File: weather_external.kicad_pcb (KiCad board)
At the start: 2 copper layers, 28.2 x 51.6 mm, 31 parts, among them J1 Conn_01x02_Male, J2 USB_B_Mini, J3 Conn_01x02_Male, J4 Conn_01x02_Male, J8 FTDI, Q1 DMG2305UX-13, SW1 SW_Push, U1 MCP73831-2-OT, U2 MCP1700T-3302E_TT

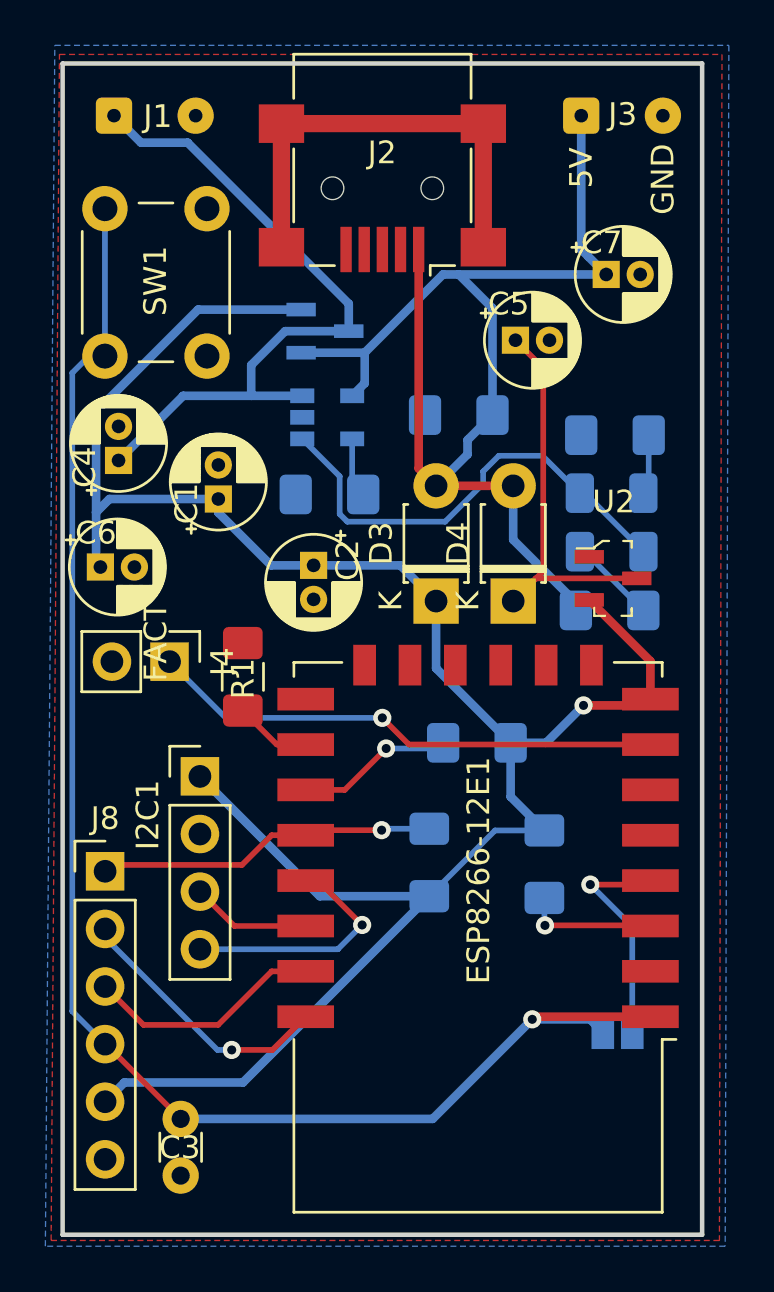
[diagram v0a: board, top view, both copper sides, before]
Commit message: V1.5 removing battery charger components
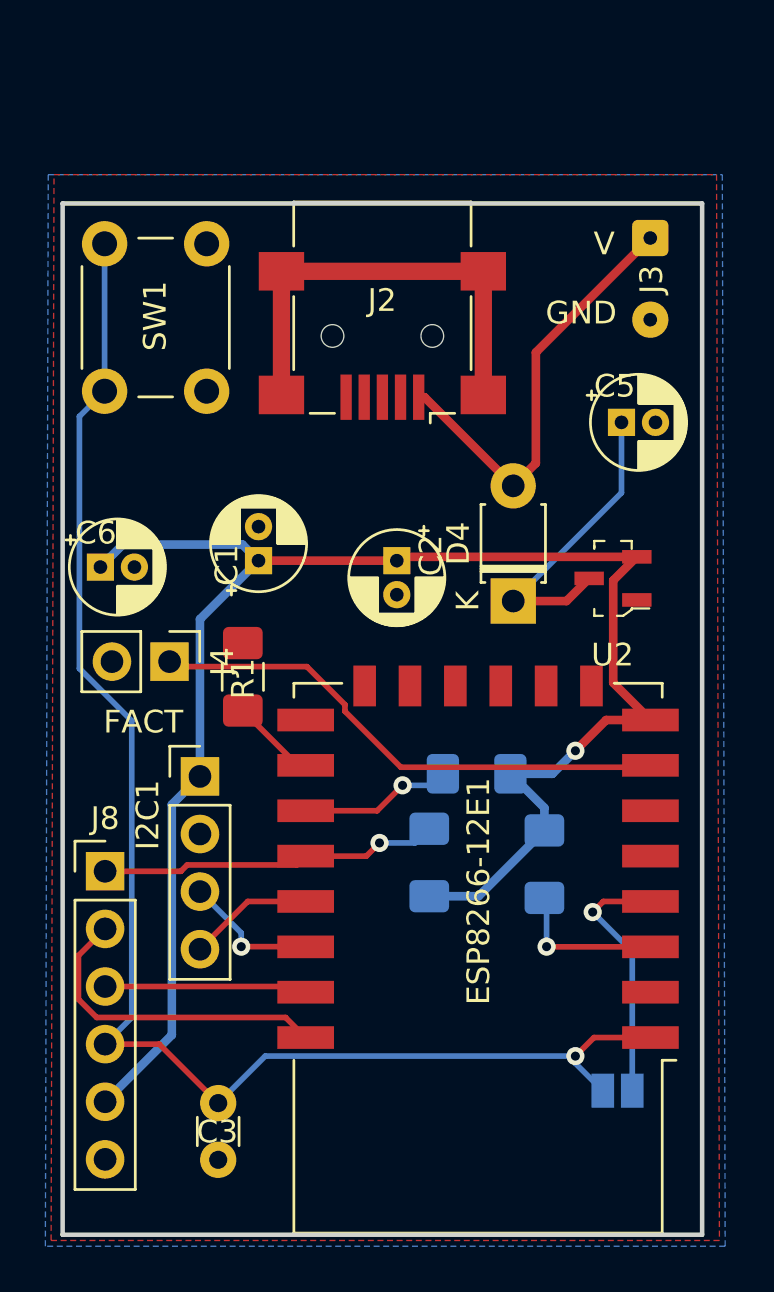
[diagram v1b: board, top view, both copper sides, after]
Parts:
- removed C4, C7: CP, Capacitor_THT:CP_Radial_D4.0mm_P1.50mm
- removed D1: GREEN, LED_SMD:LED_1206_3216Metric
- removed D2: RED, LED_SMD:LED_1206_3216Metric
- removed D3: 1N4148, Diode_THT:D_T-1_P5.08mm_Horizontal
- removed J1: Conn_01x02_Male, Connector_Wire:SolderWire-0.1sqmm_1x02_P3.6mm_D0.4mm_OD1mm
- removed Q1: DMG2305UX-13, digikey-footprints:SOT-23-3
- removed R5, R6: 220, Resistor_SMD:R_1206_3216Metric_Pad1.42x1.75mm_HandSolder
- removed R7: 2k, Resistor_SMD:R_1206_3216Metric_Pad1.42x1.75mm_HandSolder
- removed R8: 100k, Resistor_SMD:R_1206_3216Metric_Pad1.42x1.75mm_HandSolder
- removed U1: MCP73831-2-OT, Package_TO_SOT_SMD:SOT-23-5
- moved J2 6.51 mm to (10.0, 57.9)
- moved J3 6.19 mm to (21.8, 53.6), turned to 270 degrees
- moved C5 5.91 mm to (20.6, 61.7)
- moved C2 3.67 mm to (10.7, 67.8)
- moved C1 3.24 mm to (4.57, 67.8)
- moved JP1 2.59 mm to (20.4, 91.2)
- moved C3 1.79 mm to (2.79, 94.2)
- moved SW1 1.55 mm to (2.29, 53.8)
- moved R4 1.37 mm to (14.2, 77.2)
- moved ESP8266-12E1 0.92 mm to (14.2, 85.3)
- turned U2 to 180 degrees
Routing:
- net VCC: track 56.2 -> 19.2 mm
- net VBAT: track 30.5 -> 0.00 mm
- net Net-(D1-Pad2): track 20.8 -> 0.00 mm
- net +3V3: track 96.7 -> 75.9 mm
- net SDA: track 10.9 -> 5.53 mm, vias 1 -> 0
- net Net-(C5-Pad1): track 18.4 -> 13.6 mm
- net Net-(D2-Pad2): track 3.87 -> 0.00 mm
- net RST: track 69.3 -> 65.6 mm
- net Net-(D1-Pad1): track 2.65 -> 0.00 mm
- net Net-(R7-Pad2): track 2.65 -> 0.00 mm
- net TX: track 12.4 -> 14.3 mm, vias 1 -> 0
- net RX: track 10.5 -> 8.95 mm
- net GPIO16: track 9.99 -> 11.3 mm
- net EN: track 5.88 -> 6.77 mm
- net SCL: track 5.29 -> 6.02 mm, vias 0 -> 1
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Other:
- board size 28.2 x 51.6 mm -> 28.2 x 45.5 mm
- board text added: "Weather External v1.5"
- board text removed: "3V3"
- board text removed: "5V"
- board text removed: "SOLAR PANEL"
- board text removed: "Weather External v1.4"

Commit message: V 1.5 - no load management once it is built to run in solar panel charging mode
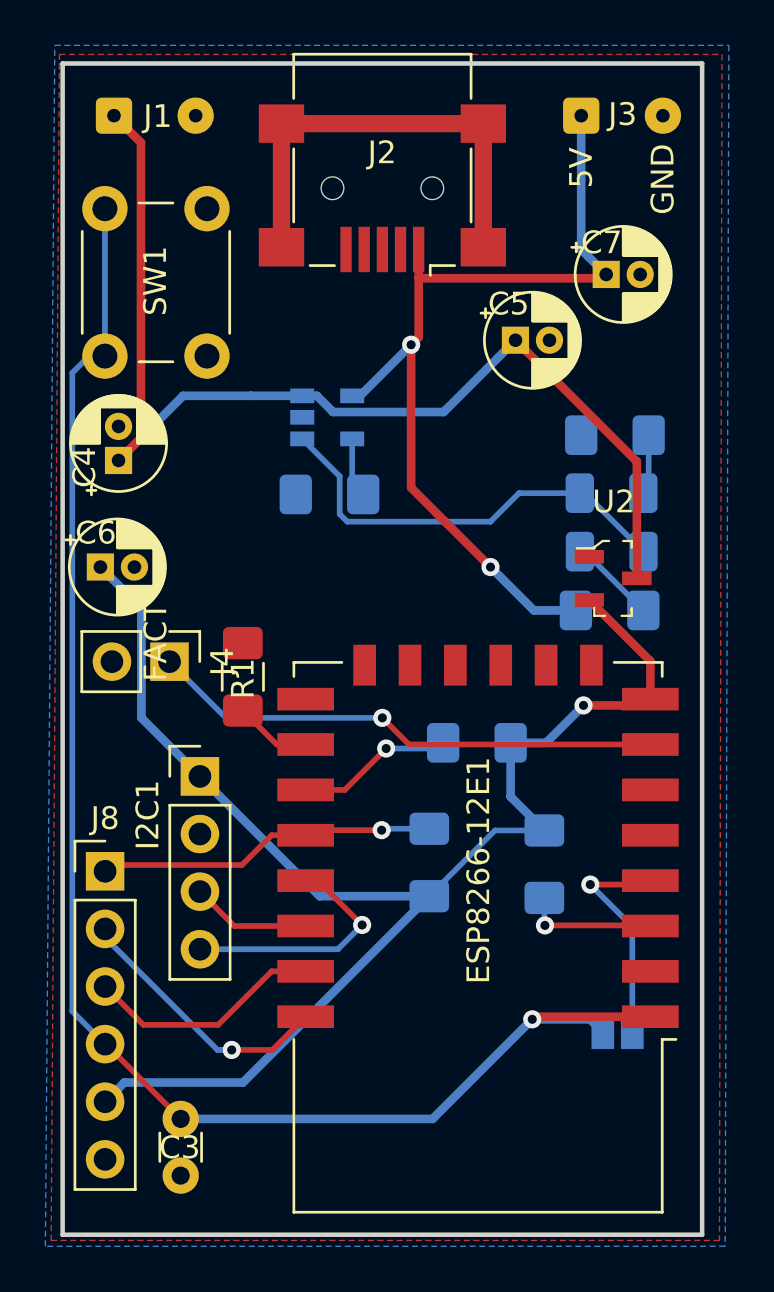
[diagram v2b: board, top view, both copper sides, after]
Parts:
- removed C1: 0.1uf, Capacitor_THT:CP_Radial_D4.0mm_P1.50mm
- removed C2: 47uf, Capacitor_THT:CP_Radial_D4.0mm_P1.50mm
- removed D4: 1N4148, Diode_THT:D_T-1_P5.08mm_Horizontal
- added C4: CP, Capacitor_THT:CP_Radial_D4.0mm_P1.50mm, F.Cu at (-1.60, 63.4)
- added C7: CP, Capacitor_THT:CP_Radial_D4.0mm_P1.50mm, F.Cu at (19.9, 55.2)
- added D1: GREEN, LED_SMD:LED_1206_3216Metric, B.Cu at (20.1, 64.8)
- added D2: RED, LED_SMD:LED_1206_3216Metric, B.Cu at (20.1, 67.4)
- added J1: Battery, Connector_Wire:SolderWire-0.1sqmm_1x02_P3.6mm_D0.4mm_OD1mm, F.Cu at (-1.80, 48.2)
- added R5: 220, Resistor_SMD:R_1206_3216Metric_Pad1.42x1.75mm_HandSolder, B.Cu at (20.3, 62.3)
- added R6: 220, Resistor_SMD:R_1206_3216Metric_Pad1.42x1.75mm_HandSolder, B.Cu at (20.1, 70.0)
- added R7: 2k, Resistor_SMD:R_1206_3216Metric_Pad1.42x1.75mm_HandSolder, B.Cu at (7.70, 64.9)
- added U1: MCP73831-2-OT, Package_TO_SOT_SMD:SOT-23-5, B.Cu at (7.60, 61.5)
- J3: value Conn_01x02_Male -> Solar Panel
- moved J2 6.51 mm to (10.0, 51.4)
- moved J3 6.19 mm to (18.8, 48.2), turned to 0 degrees
- moved C5 5.91 mm to (15.9, 58.1)
- moved JP1 2.59 mm to (20.4, 88.6)
- moved C3 1.79 mm to (1.14, 94.9)
- moved SW1 1.55 mm to (2.30, 52.3)
- moved R4 1.37 mm to (14.2, 75.8)
- moved ESP8266-12E1 0.92 mm to (14.2, 84.4)
- turned U2 to 0 degrees
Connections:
- net Net-(C5-Pad1) renamed VBAT
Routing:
- net VBAT: track 13.6 -> 49.1 mm
- net VCC: track 19.2 -> 39.7 mm, vias 0 -> 2
- net Net-(D1-Pad2): track 0.00 -> 19.1 mm
- net +3V3: track 75.9 -> 64.9 mm
- net SDA: track 5.53 -> 10.9 mm, vias 0 -> 1
- net Net-(D2-Pad2): track 0.00 -> 3.87 mm
- net RST: track 65.6 -> 69.3 mm
- net Net-(D1-Pad1): track 0.00 -> 2.65 mm
- net Net-(R7-Pad2): track 0.00 -> 2.65 mm
- net TX: track 14.3 -> 12.4 mm, vias 0 -> 1
- net RX: track 8.95 -> 10.5 mm
- net GPIO16: track 11.3 -> 9.99 mm
- net EN: track 6.77 -> 5.88 mm
- net SCL: track 6.02 -> 5.29 mm, vias 1 -> 0
- net GPIO13: track 23.3 -> 22.7 mm, vias 0 -> 1
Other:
- board size 28.2 x 45.5 mm -> 28.2 x 51.6 mm
- board text added: "3V3"
- board text added: "5V"
- board text added: "SOLAR PANEL"
